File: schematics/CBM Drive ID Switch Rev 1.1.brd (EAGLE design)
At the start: 20.3 x 53.3 mm, 20 parts, among them IC1 MOS6522, IC2 ATMEGA48, IC3 2x20pin headers, IC4 74AHCT273, IC5 741G04, Y1 20MHz

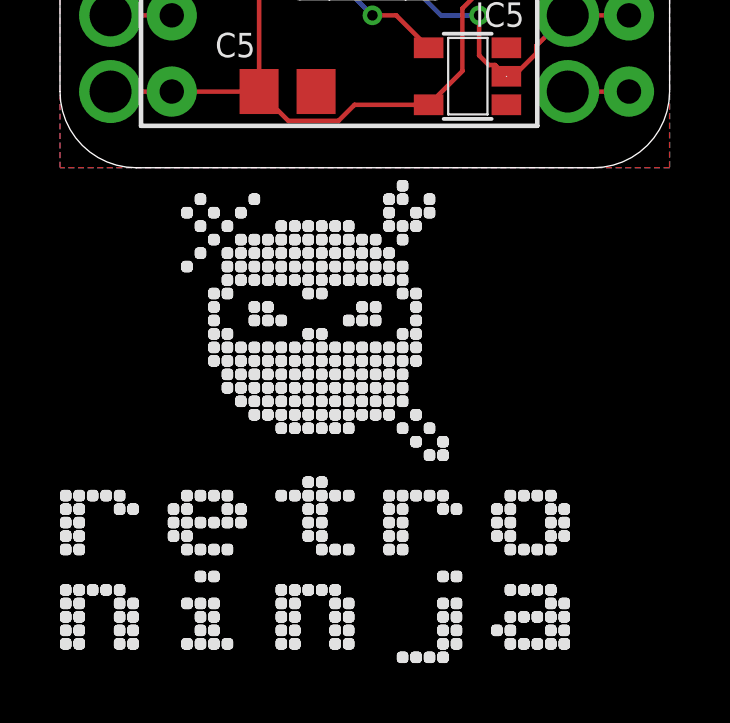
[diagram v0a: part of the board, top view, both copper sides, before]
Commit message: Schematics corrected
Pin names corrected. Informational change only
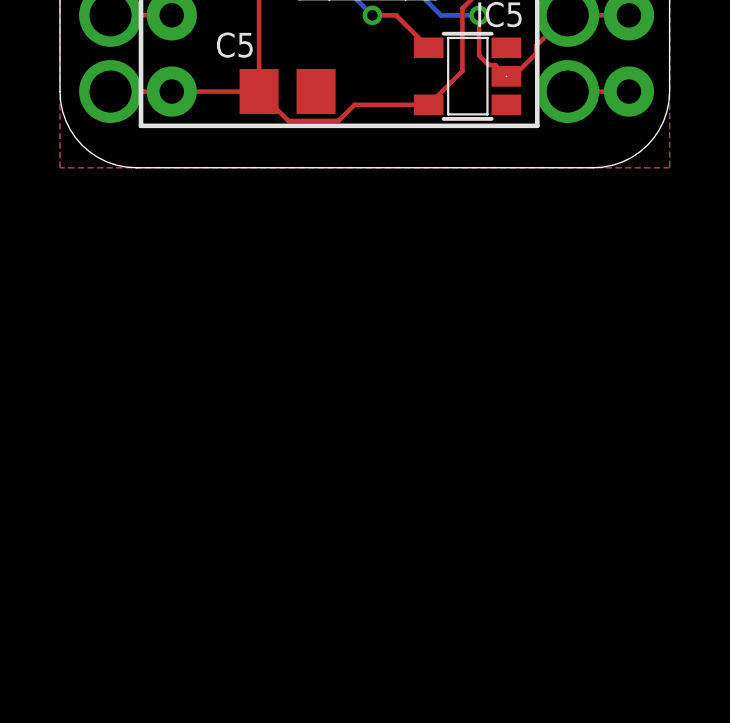
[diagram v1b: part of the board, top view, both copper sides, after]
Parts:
- removed U$3: RETRONINJA_17MM, Graphics:RETRONINJA_17MM
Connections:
- removed net CA0: IC1.40, IC3.40
- removed net CB0: IC1.18, IC3.18
- new net CA2: IC1.39, IC3.39
- new net CB2: IC1.19, IC3.19
- net CA1: now also IC1.40, IC3.40; no longer IC1.39, IC3.39
- net CB1: now also IC1.18, IC3.18; no longer IC1.19, IC3.19
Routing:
- net CB2: track 0.00 -> 2.04 mm
- net CB0: track 2.04 -> 0.00 mm
- net CA2: track 0.00 -> 2.04 mm
- net CA0: track 2.04 -> 0.00 mm
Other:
- board text added: "Retroninja ID Switch for CBM disk drives Rev 1b"
- board text removed: "Retroninja ID Switch for CBM disk drives Rev 1"
